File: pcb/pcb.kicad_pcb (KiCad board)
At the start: 2 copper layers, 115.2 x 76.8 mm, 62 parts, among them J1 TYPE-C-31-M-12, J2 AudioJack4, J3 AudioJack4, SW1 SW_Push, SW10 SW_Push, SW11 SW_Push, SW12 SW_Push, SW13 SW_Push, SW14 SW_Push, SW15 SW_Push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

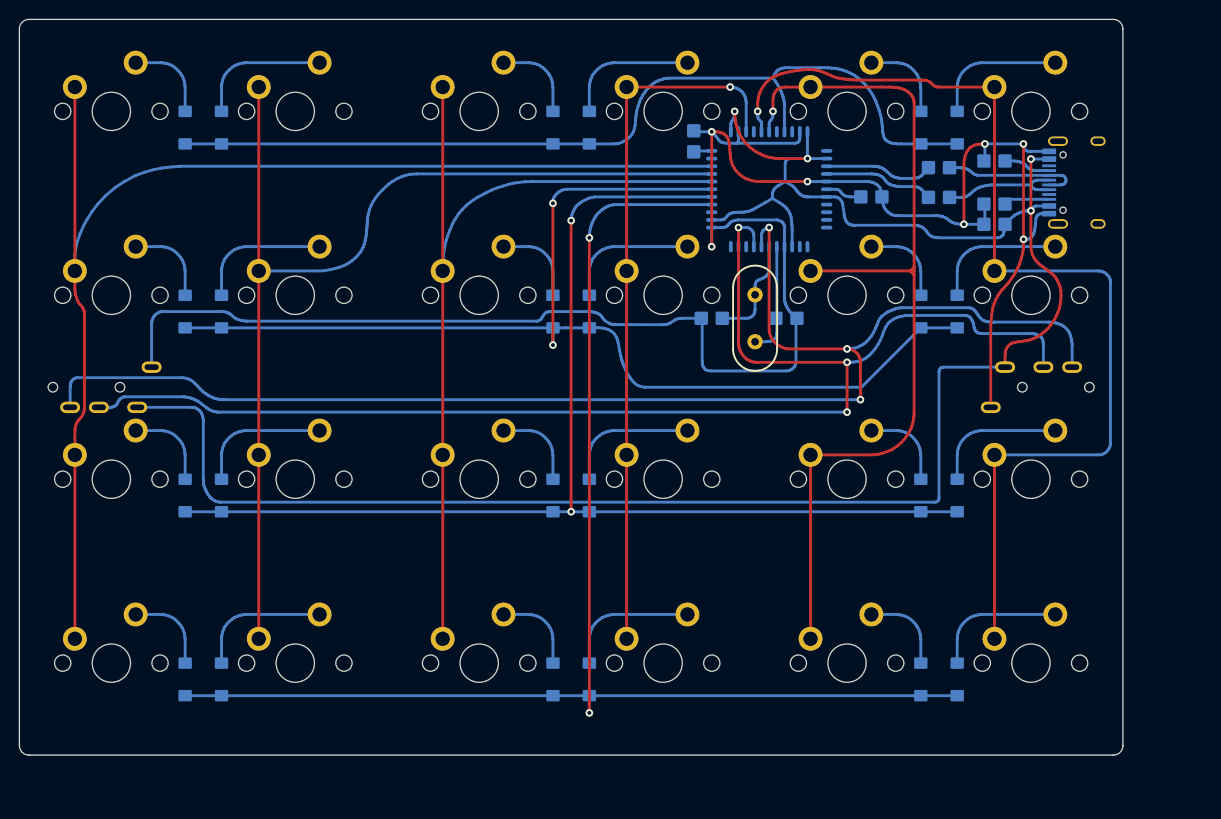
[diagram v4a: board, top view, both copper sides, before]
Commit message: audio connector offset
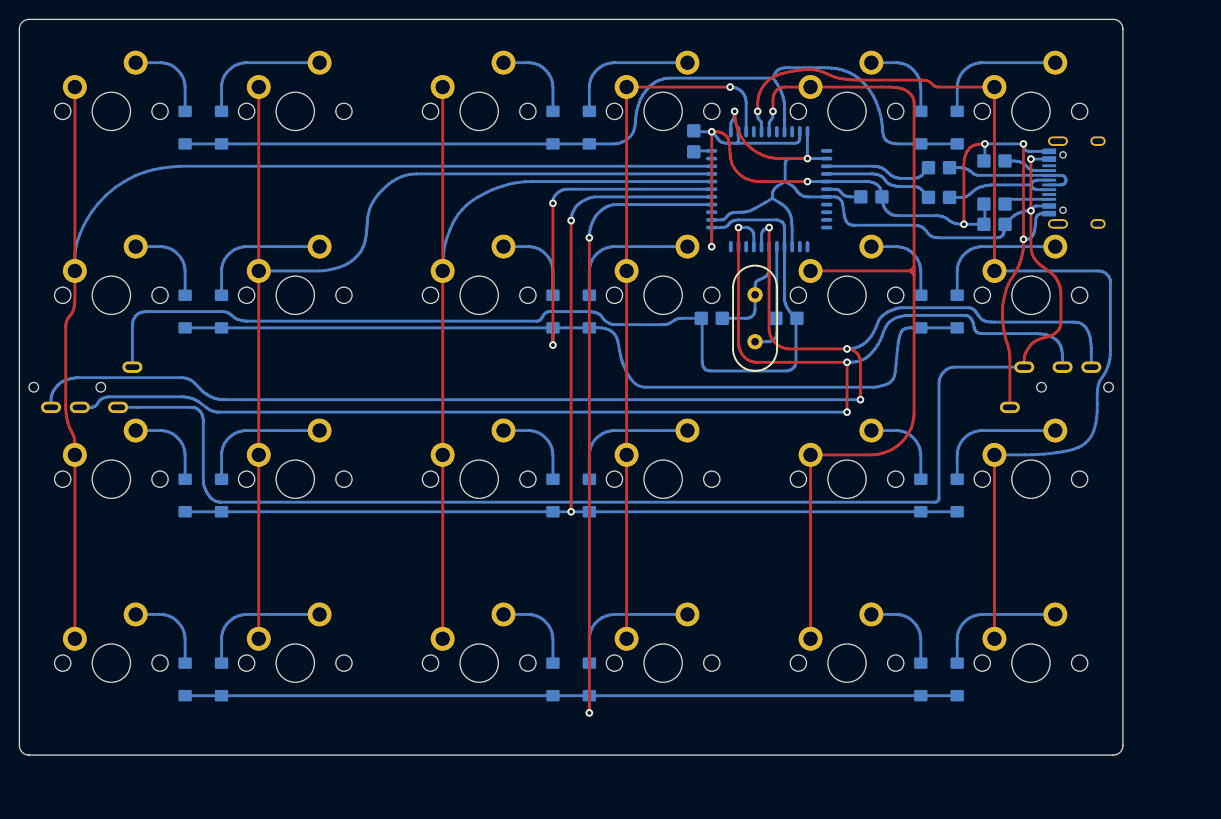
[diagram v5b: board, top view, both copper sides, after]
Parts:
- moved J2 2.00 mm to (117.2, 38.4)
- moved J3 2.00 mm to (-2.00, 38.4)
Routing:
- net SDA: track 139.0 -> 142.4 mm
- net SCL: track 144.2 -> 147.5 mm
- net C5: track 110.8 -> 108.3 mm
- net VCC: track 210.6 -> 212.8 mm
- net R1: track 121.0 -> 123.0 mm
- net GND: track 218.2 -> 219.8 mm
